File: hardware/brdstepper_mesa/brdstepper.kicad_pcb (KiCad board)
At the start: 4 copper layers, 28 x 28 mm, 88 parts, among them J2 VM / GND / EN, J3 MOTOR, J4 SMART-SERIAL, J7 SWD, U1 STM32G473CEU6, U2 DRV8876RGTR, U3 DRV8876RGTR, U4 AS5047P-ATSM, U5 TLV75533PDBVR, U6 TPS560430XDBVR, U7 USBLC6-2SC6, U8 SN65HVD30DR, Y1 8MHz

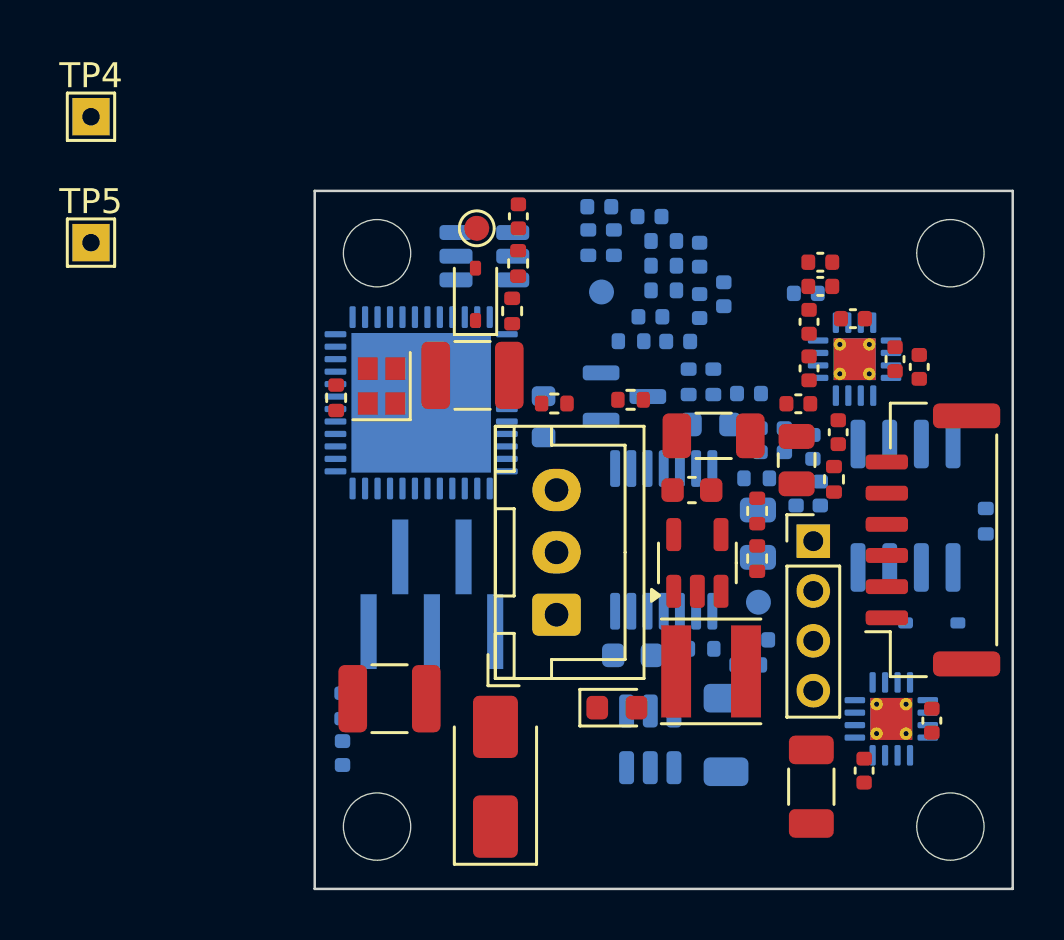
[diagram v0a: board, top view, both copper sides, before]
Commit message: brdstepper: split into serial and CAN boards, 0603 passives (WIP, not routed)
- hardware/brdstepper_common: shared parts/board definitions built per
  variant; brdstepper_mesa (A, smart-serial) and brdstepper_can (B, CAN)
  each fit only their own interface parts, MCU pins of the other
  interface left open, HWID divider per variant.
- 0402 resistors and capacitors become 0603; power capacitors stay larger.
- kigen place: GAP_MAX bisects the largest courtyard gap that still
  places every part (0603 on 28 x 28 mm only just fits: gap ~0).
- kigen route: DSN export, BrdRoute, SES import, zone fill (untested end
  to end: first router run still going).

Not done yet: routing on 4 layers, READMEs/BOMs/renders refresh, DEBUGNOTES.

Co-Authored-By: Claude Sonnet 5.5 <noreply@anthropic.com>
Claude-Session: https://claude.ai/code/session_017CSpK2B8oMBAmr39Kq1RSC
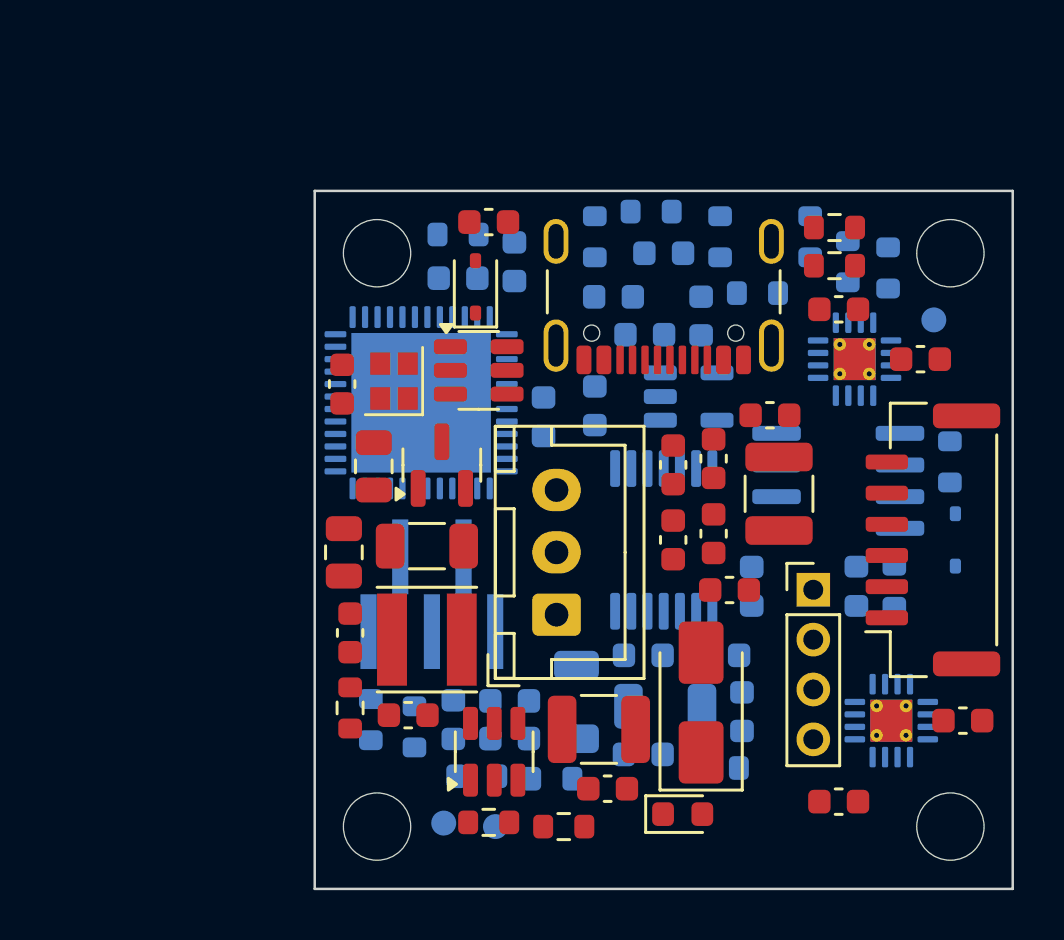
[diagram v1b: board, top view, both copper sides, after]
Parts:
- removed R7: 10k, Resistor_SMD:R_0402_1005Metric
- removed TP4, TP5: TestPoint, TestPoint:TestPoint_THTPad_1.5x1.5mm_Drill0.7mm
- added J1: USB-C, Connector_USB:USB_C_Receptacle_GCT_USB4105-xx-A_16P_TopMnt_Horizontal, F.Cu at (100.0, 89.1)
- C10, C12, C13, C17, C19, C22: footprint Capacitor_SMD:C_0402_1005Metric -> Capacitor_SMD:C_0603_1608Metric; moved to F.Cu
- C11, C14, C15, C16, C18, C20, C25, C26, C27, C29, C30, C31, C32, C33, C36, C37, C38, C5, C9: footprint Capacitor_SMD:C_0402_1005Metric -> Capacitor_SMD:C_0603_1608Metric
- C21, C3, TP2, U5: moved to B.Cu
- C23, C34, C4, C8: footprint Capacitor_SMD:C_0402_1005Metric -> Capacitor_SMD:C_0603_1608Metric; moved to B.Cu
- C35, C6, D1, U6, U7: moved to F.Cu
- R1, R13, R14, R18, R19, R2, R20, R5, R9: footprint Resistor_SMD:R_0402_1005Metric -> Resistor_SMD:R_0603_1608Metric
- R10, R11, R12, R15, R16, R3: footprint Resistor_SMD:R_0402_1005Metric -> Resistor_SMD:R_0603_1608Metric; moved to B.Cu
- R17, R4, R6: footprint Resistor_SMD:R_0402_1005Metric -> Resistor_SMD:R_0603_1608Metric; moved to F.Cu
- R8: value 10k -> 0; footprint Resistor_SMD:R_0402_1005Metric -> Resistor_SMD:R_0603_1608Metric
- moved TP2 23.9 mm to (91.2, 111.4)
- moved C38 23.9 mm to (89.8, 107.0)
- moved TP3 21.9 mm to (93.2, 111.5)
- moved R8 21.6 mm to (95.5, 109.6), turned to 0 degrees
- moved C9 21.5 mm to (93.8, 108.0)
- moved R4 20.1 mm to (93.0, 111.3)
- moved C34 19.4 mm to (93.8, 106.5), turned to 0 degrees
- moved C8 19.1 mm to (99.2, 108.6), turned to 0 degrees
- moved R6 18.5 mm to (96.0, 111.5), turned to 0 degrees
- moved C4 18.3 mm to (103.1, 106.9), turned to 90 degrees
- moved C28 18.2 mm to (90.5, 100.2), turned to 0 degrees
- moved R1 17.4 mm to (87.4, 106.7)
- moved C7 17.0 mm to (88.4, 97.0)
- moved C6 16.6 mm to (87.2, 100.5)
- moved TP1 13.3 mm to (110.8, 91.2)
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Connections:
- net /3V3 renamed 3V3
- net /5V renamed 5V
- net /5V_BUCK renamed 5V_BUCK
- net /5V_MESA renamed 5V_MESA
- net /5V_USB renamed 5V_USB
- net /AIN renamed AIN
- net /AIN_IN renamed AIN_IN
- net /A_IN1 renamed A_IN1
- net /A_IN2 renamed A_IN2
- net /BUCK_CB renamed BUCK_CB
- net /BUCK_FB renamed BUCK_FB
- net /BUCK_SW renamed BUCK_SW
- net /B_IN1 renamed B_IN1
- net /B_IN2 renamed B_IN2
- net /CAN_RX renamed CAN_RX
- net /COIL_A+ renamed COIL_A+
- net /COIL_A- renamed COIL_A-
- net /COIL_B+ renamed COIL_B+
- net /COIL_B- renamed COIL_B-
- net /ENC_CLK renamed ENC_CLK
- net /ENC_CS renamed ENC_CS
- net /ENC_MISO renamed ENC_MISO
- net /ENC_MOSI renamed ENC_MOSI
- net /EN_IN renamed EN_IN
- net /EN_RAW renamed EN_RAW
- net /GND renamed GND
- net /HWID renamed HWID
- net /IPROPI_A renamed IPROPI_A
- net /IPROPI_B renamed IPROPI_B
- net /LED renamed LED
- net /LED_A renamed LED_A
- net /NRST renamed NRST
- net /NTC renamed NTC
- net /OSC_IN renamed OSC_IN
- net /OSC_OUT renamed OSC_OUT
- net /SS_RX renamed SS_RX
- net /SS_RX+ renamed SS_RX+
- net /SS_RX- renamed SS_RX-
- net /SS_TX renamed SS_TX
- net /SS_TX+ renamed SS_TX+
- net /SS_TX- renamed SS_TX-
- net /SWCLK renamed SWCLK
- net /SWDIO renamed SWDIO
- net /TP_PB10 renamed TP_PB10
- net /TP_PB11 renamed TP_PB11
- net /U2_CPH renamed U2_CPH
- net /U2_CPL renamed U2_CPL
- net /U2_VCP renamed U2_VCP
- net /U3_CPH renamed U3_CPH
- net /U3_CPL renamed U3_CPL
- net /U3_VCP renamed U3_VCP
- net /USB_DM renamed USB_DM
- net /USB_DP renamed USB_DP
- net /USB_SHIELD renamed USB_SHIELD
- net /VDDA renamed VDDA
- net /VM renamed VM
- net /VM_SENSE renamed VM_SENSE
- net /VREF_DRV renamed VREF_DRV
- net /nFAULT renamed nFAULT
- net /nSLEEP renamed nSLEEP
- R17 pad 1: /USB_CC1 -> USB_CC1
- R18 pad 1: /USB_CC2 -> USB_CC2
- U1 pad 16: unconnected-(U1-PC4-Pad16) -> (no net)
- U1 pad 19: unconnected-(U1-PB2-Pad19) -> (no net)
- U1 pad 2: unconnected-(U1-PC13-Pad2) -> (no net)
- U1 pad 26: /CAN_STB -> (no net)
- U1 pad 27: unconnected-(U1-PB14-Pad27) -> (no net)
- U1 pad 28: unconnected-(U1-PB15-Pad28) -> (no net)
- U1 pad 3: unconnected-(U1-PC14-Pad3) -> (no net)
- U1 pad 39: unconnected-(U1-PC10-Pad39) -> (no net)
- U1 pad 4: unconnected-(U1-PC15-Pad4) -> (no net)
- U1 pad 40: unconnected-(U1-PC11-Pad40) -> (no net)
- U1 pad 47: /CAN_TX -> (no net)
- U2 pad 5: unconnected-(U2-IMODE-Pad5) -> (no net)
- U3 pad 5: unconnected-(U3-IMODE-Pad5) -> (no net)
- U4 pad 10: unconnected-(U4-U-Pad10) -> (no net)
- U4 pad 14: unconnected-(U4-I/PWM-Pad14) -> (no net)
- U4 pad 6: unconnected-(U4-B-Pad6) -> (no net)
- U4 pad 7: unconnected-(U4-A-Pad7) -> (no net)
- U4 pad 8: unconnected-(U4-W/PWM-Pad8) -> (no net)
- U4 pad 9: unconnected-(U4-V-Pad9) -> (no net)
- U5 pad 4: unconnected-(U5-NC-Pad4) -> (no net)

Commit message: brdstepper: spread pass, BrdRoute step with own SES import (WIP)
- kigen place: SPREAD pushes parts apart into the room left after the
  gap search (serial board: 67.3% -> 79.2% routed in a 150 s run).
- kigen route: DSN export, boundary inset by the edge clearance,
  BrdRoute, own SES importer (pcbnew's ImportSpecctraSES needs the
  editor), zone fill.
- Power net class 0.3 mm / 0.15 mm clearance / 0.6 mm vias for this board
  (the 0.5 / 0.2 / 0.8 mm default did not match what the router was given).

Boards are a snapshot taken while a routing run was in progress: still
not fully routed, DRC not clean.

Co-Authored-By: Claude Sonnet 5.5 <noreply@anthropic.com>
Claude-Session: https://claude.ai/code/session_017CSpK2B8oMBAmr39Kq1RSC
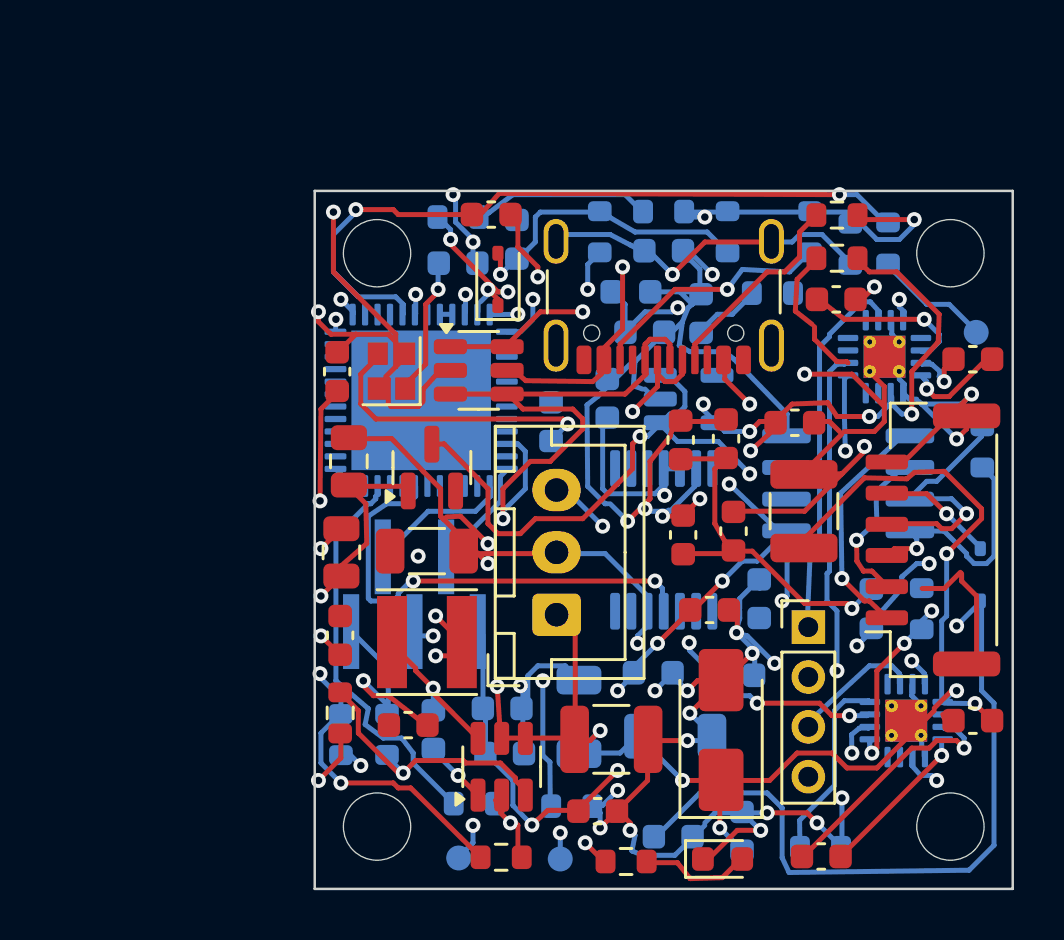
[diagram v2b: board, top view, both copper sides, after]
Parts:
- moved R12 5.20 mm to (106.3, 112.3)
- moved C4 4.80 mm to (103.1, 111.7)
- moved C8 3.51 mm to (100.4, 111.9)
- moved TP3 2.91 mm to (95.8, 112.8)
- moved R6 2.87 mm to (98.5, 112.9)
- moved D4 2.41 mm to (102.4, 112.8)
- moved C30 2.31 mm to (106.3, 112.7)
- moved C26 2.10 mm to (112.4, 92.8)
- moved TP1 1.77 mm to (112.5, 91.7)
- moved D3 1.72 mm to (112.7, 101.4)
- moved TP2 1.52 mm to (91.8, 112.8)
- moved J3 1.51 mm to (105.8, 103.5)
- moved R4 1.49 mm to (93.5, 112.7)
- moved R20 1.43 mm to (112.8, 96.3)
- moved R13 1.42 mm to (110.3, 102.8)
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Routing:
- net GND: track 0.00 -> 266.2 mm, vias 0 -> 37
- net 3V3: track 0.00 -> 92.3 mm, vias 0 -> 19
- net VM: track 0.00 -> 74.2 mm, vias 0 -> 10
- net 5V: track 0.00 -> 60.4 mm, vias 0 -> 3
- net nSLEEP: track 0.00 -> 42.8 mm, vias 0 -> 5
- net VREF_DRV: track 0.00 -> 29.1 mm, vias 0 -> 4
- net AIN: track 0.00 -> 28.9 mm, vias 0 -> 2
- net LED: track 0.00 -> 25.9 mm, vias 0 -> 2
- net 5V_BUCK: track 0.00 -> 25.0 mm, vias 0 -> 4
- net VM_SENSE: track 0.00 -> 24.4 mm, vias 0 -> 3
- net USB_DP: track 0.00 -> 24.3 mm, vias 0 -> 1
- net nFAULT: track 0.00 -> 23.8 mm, vias 0 -> 2
- net TP_PB10: track 0.00 -> 23.8 mm, vias 0 -> 2
- net TP_PB11: track 0.00 -> 23.8 mm, vias 0 -> 2
- net HWID: track 0.00 -> 23.6 mm, vias 0 -> 3
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
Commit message: brdstepper: USB and SWD as test pads, motor pads on the edge, plane fanout (WIP)
- USB-C connector, its CC/shield parts and ESD chip replaced by four test
  pads (5V, D+, D-, GND) on both boards; SWD header by five test pads.
- Motor pads J3 fixed on the north edge of both boards.
- All fixed parts (the encoder on the shaft axis, holes, edge connectors)
  are locked in the generated board.
- Placement is much looser without the two connectors: serial board
  courtyard gap 0.30 mm.
- kigen route: loads a bare board (pcbnew 7 crashes when tracks are
  removed), GND plane fanout (a via + stub per SMD pad, vias in the MCU's
  exposed pad), In1 hidden from the router, router exit code ignored when
  a session was written.
- DEBUGNOTES: headless pcbnew gotchas.

Needs the BrdRoute plane-net change (not yet committed there); boards are
a routing snapshot, not complete.

Co-Authored-By: Claude Sonnet 5.5 <noreply@anthropic.com>
Claude-Session: https://claude.ai/code/session_017CSpK2B8oMBAmr39Kq1RSC
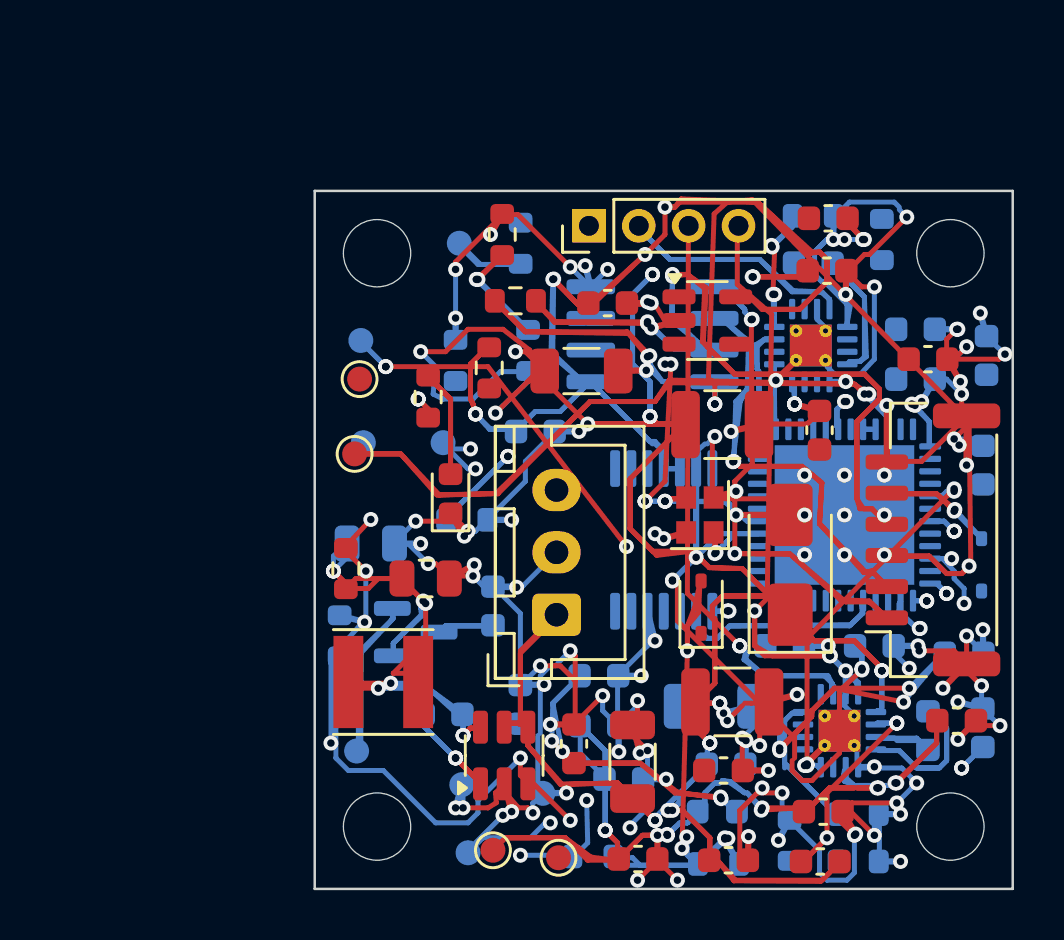
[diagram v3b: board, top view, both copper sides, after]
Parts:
- removed C37: 4.7n, Capacitor_SMD:C_0603_1608Metric
- removed J1: USB-C, Connector_USB:USB_C_Receptacle_GCT_USB4105-xx-A_16P_TopMnt_Horizontal
- removed J7: SWD, Connector_PinHeader_1.27mm:PinHeader_1x05_P1.27mm_Vertical_SMD_Pin1Left
- removed R17, R18: 5.1k, Resistor_SMD:R_0603_1608Metric
- removed R19: 1M, Resistor_SMD:R_0603_1608Metric
- removed U7: USBLC6-2SC6, Package_TO_SOT_SMD:SOT-23-6
- added TP10: USB D+, TestPoint:TestPoint_Pad_D1.0mm, B.Cu at (91.2, 96.1)
- added TP11: USB D-, TestPoint:TestPoint_Pad_D1.0mm, F.Cu at (95.8, 112.8)
- added TP12: USB GND, TestPoint:TestPoint_Pad_D1.0mm, B.Cu at (95.2, 110.2)
- added TP4: SWD 3V3, TestPoint:TestPoint_Pad_D1.0mm, F.Cu at (93.2, 112.5)
- added TP5: SWDIO, TestPoint:TestPoint_Pad_D1.0mm, B.Cu at (87.8, 92.0)
- added TP6: NRST, TestPoint:TestPoint_Pad_D1.0mm, B.Cu at (88.0, 96.1)
- added TP7: SWCLK, TestPoint:TestPoint_Pad_D1.0mm, B.Cu at (92.2, 112.5)
- added TP8: SWD GND, TestPoint:TestPoint_Pad_D1.0mm, B.Cu at (91.9, 109.8)
- added TP9: USB 5V, TestPoint:TestPoint_Pad_D1.0mm, B.Cu at (87.7, 108.5)
- C11, C12, C17, C20, C22, C26, C28, C30, C38, C7, D1: moved to B.Cu
- C16, C18, C21, C24, C27, C3, C9, R20, TP2, TP3, U5: moved to F.Cu
- moved C36 27.1 mm to (112.8, 107.5)
- moved C17 26.7 mm to (112.8, 97.0)
- moved R16 25.4 mm to (102.2, 113.0), turned to 0 degrees
- moved R15 25.1 mm to (97.2, 112.7), turned to 0 degrees
- moved R4 25.0 mm to (93.5, 87.8), turned to 90 degrees
- moved C14 23.7 mm to (110.6, 92.8), turned to 0 degrees
- moved C27 23.1 mm to (102.6, 112.8)
- moved C15 22.7 mm to (108.5, 104.2)
- moved TP1 21.0 mm to (91.8, 88.1)
- moved TP3 20.9 mm to (87.8, 93.5)
- moved C35 20.4 mm to (97.8, 90.5)
- moved R6 20.3 mm to (90.5, 94.3), turned to 90 degrees
- moved R20 19.6 mm to (94.0, 90.4), turned to 0 degrees
- moved J3 18.3 mm to (97.0, 87.4), turned to 90 degrees
- moved D4 18.3 mm to (91.5, 98.2), turned to 90 degrees
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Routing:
- net VM: track 74.2 -> 188.9 mm, vias 10 -> 21
- net SS_RX+: track 9.99 -> 85.3 mm, vias 1 -> 5
- net 5V: track 60.4 -> 4.74 mm, vias 3 -> 0
- net SWDIO: track 4.54 -> 57.4 mm, vias 0 -> 6
- net SS_RX-: track 10.4 -> 58.7 mm, vias 1 -> 4
- net 3V3: track 92.3 -> 139.6 mm, vias 19 -> 16
- net EN_IN: track 12.2 -> 56.9 mm, vias 1 -> 7
- net SWCLK: track 5.75 -> 48.7 mm, vias 0 -> 4
- net COIL_B+: track 5.35 -> 45.5 mm, vias 0 -> 2
- net OSC_IN: track 5.59 -> 45.6 mm, vias 1 -> 6
- net BUCK_FB: track 11.2 -> 50.2 mm, vias 1 -> 5
- net COIL_B-: track 7.53 -> 45.7 mm, vias 1 -> 3
- net nSLEEP: track 42.8 -> 5.26 mm, vias 5 -> 0
- net B_IN2: track 0.00 -> 30.2 mm, vias 0 -> 4
- net AIN: track 28.9 -> 0.00 mm, vias 2 -> 0
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
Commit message: brdstepper: re-placed boards without J2 (routing run in progress)
Both boards re-placed with J2 gone, courtyard gap 0.40 mm. Snapshot taken
while the first plane-aware routing run is still going: copper may be
missing or partial.

Co-Authored-By: Claude Sonnet 5.5 <noreply@anthropic.com>
Claude-Session: https://claude.ai/code/session_017CSpK2B8oMBAmr39Kq1RSC
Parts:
- removed J2: VM / GND / EN, Connector_JST:JST_XH_B3B-XH-A_1x03_P2.50mm_Vertical
- C11, C12, C23, C31, C33, C34, C36, C38, C7, R12, R15, TP6, TP9, U1, U2, U3: moved to F.Cu
- C14, C19, C21, C24, C27, C3, C35, D5, R14, R20, TP11, TP2, TP3, TP4, U5, Y1: moved to B.Cu
- J4: footprint Connector_JST:JST_GH_SM06B-GHS-TB_1x06-1MP_P1.25mm_Horizontal -> Connector_JST:JST_GH_SM08B-GHS-TB_1x08-1MP_P1.25mm_Horizontal
- moved C36 26.6 mm to (92.8, 90.0)
- moved R16 25.9 mm to (92.5, 89.0)
- moved R15 25.8 mm to (93.5, 87.2)
- moved R20 25.1 mm to (111.5, 108.5)
- moved R5 24.0 mm to (89.9, 96.9), turned to 90 degrees
- moved R14 23.4 mm to (112.9, 105.4)
- moved C9 21.6 mm to (89.3, 93.5), turned to 90 degrees
- moved C33 20.1 mm to (101.2, 108.9), turned to 0 degrees
- moved TP3 19.3 mm to (93.2, 112.1)
- moved TP6 18.4 mm to (96.1, 112.6)
- moved C22 17.7 mm to (92.5, 91.1)
- moved C17 17.7 mm to (95.1, 96.7), turned to 0 degrees
- moved R10 17.0 mm to (92.5, 93.2), turned to 0 degrees
- moved C15 16.7 mm to (95.6, 93.7), turned to 90 degrees
- moved C21 16.4 mm to (95.9, 103.2), turned to 90 degrees
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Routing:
- net GND: track 241.0 -> 0.00 mm, vias 109 -> 0
- net VM: track 188.9 -> 0.00 mm, vias 21 -> 0
- net 3V3: track 139.6 -> 0.00 mm, vias 16 -> 0
- net SS_RX+: track 85.3 -> 0.00 mm, vias 5 -> 0
- net SS_RX-: track 58.7 -> 0.00 mm, vias 4 -> 0
- net SWDIO: track 57.4 -> 0.00 mm, vias 6 -> 0
- net EN_IN: track 56.9 -> 0.00 mm, vias 7 -> 0
- net BUCK_FB: track 50.2 -> 0.00 mm, vias 5 -> 0
- net USB_DP: track 50.2 -> 0.00 mm, vias 4 -> 0
- net TP_PB10: track 50.2 -> 0.00 mm, vias 2 -> 0
- net SWCLK: track 48.7 -> 0.00 mm, vias 4 -> 0
- net LED: track 46.9 -> 0.00 mm, vias 4 -> 0
- net COIL_B-: track 45.7 -> 0.00 mm, vias 3 -> 0
- net OSC_IN: track 45.6 -> 0.00 mm, vias 6 -> 0
- net COIL_B+: track 45.5 -> 0.00 mm, vias 2 -> 0
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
